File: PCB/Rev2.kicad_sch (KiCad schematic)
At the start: 80 parts, among them J1 AudioJack, J2 Conn_01x03_Socket, J3 Conn_01x02_Pin, U1 TL974, U2 LM78M05, U3 SN76489, U4 TL974, U5 MCP42010, U6 SN76489

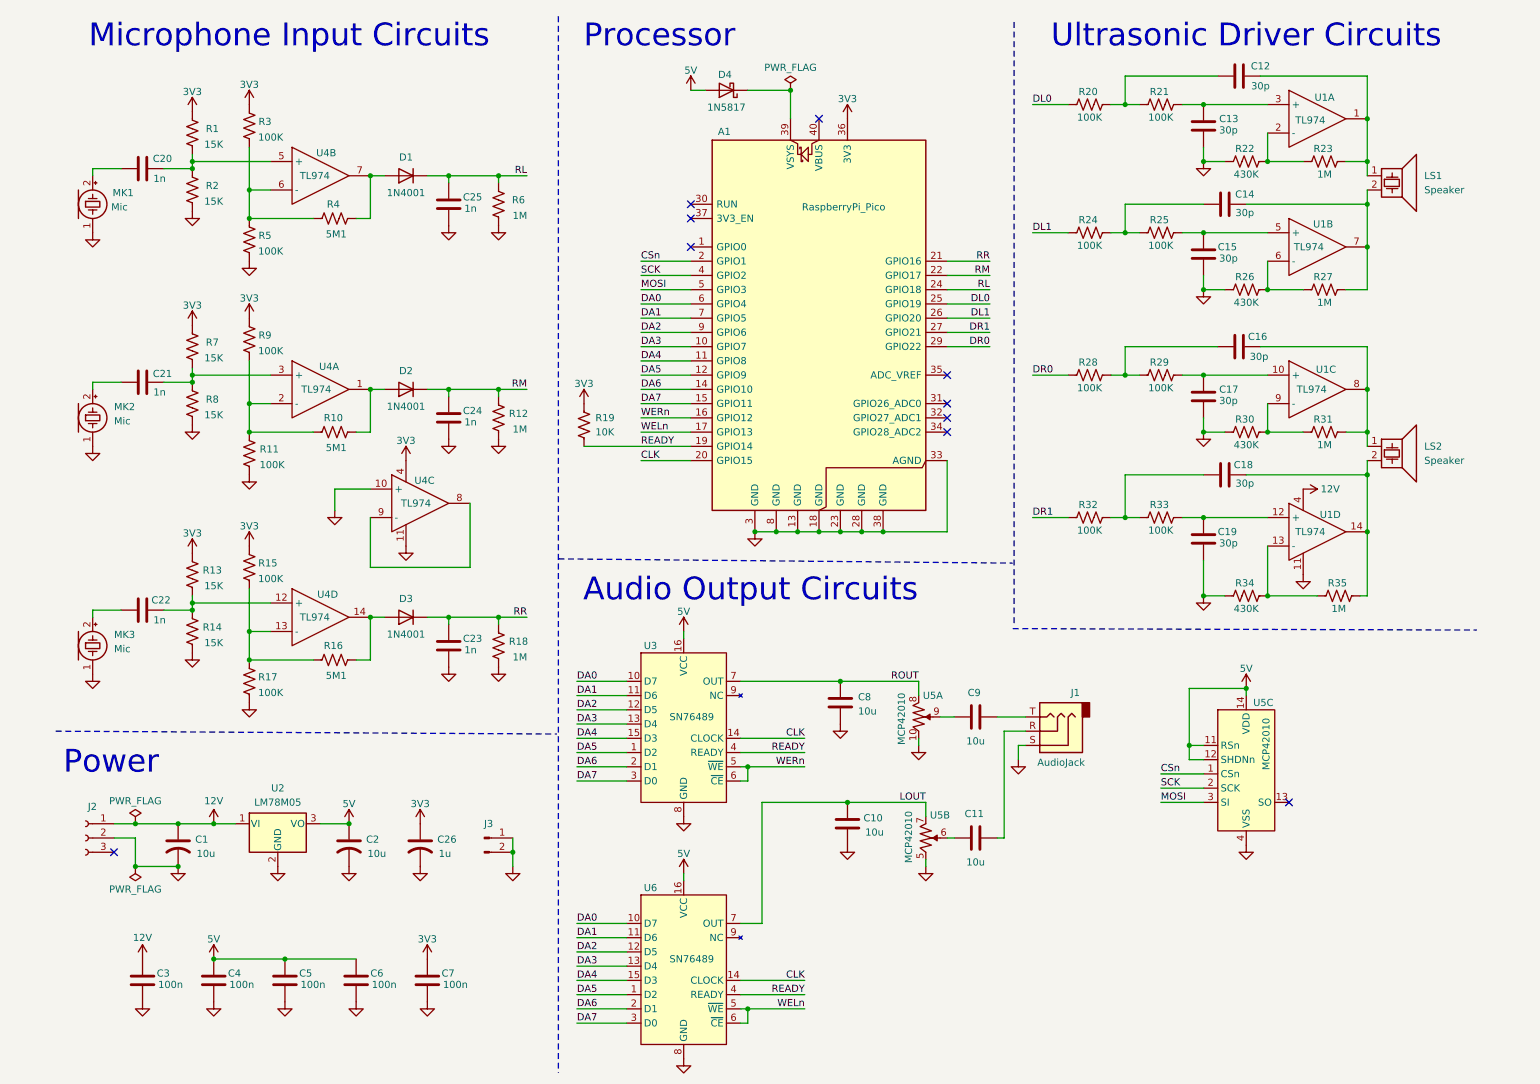
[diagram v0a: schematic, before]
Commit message: Doubled gain on receiver circuits.
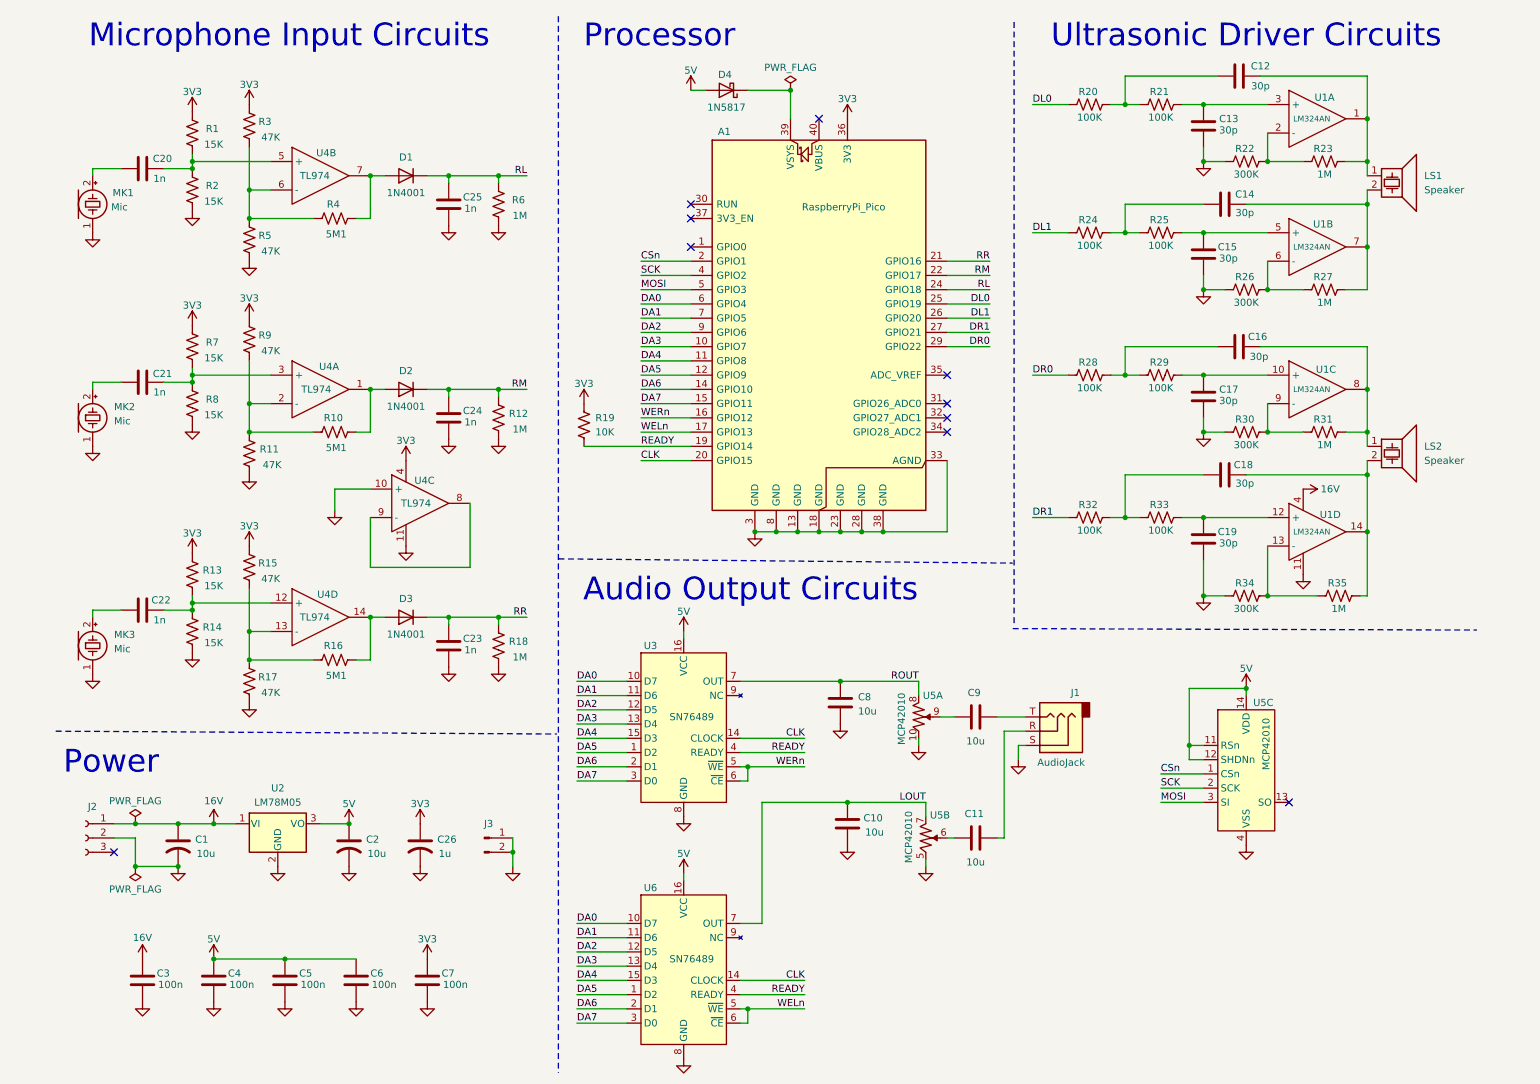
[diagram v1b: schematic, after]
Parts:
- R11, R15, R17, R3, R5, R9: value 100K -> 47K
- R22, R26, R30, R34: value 430K -> 300K
- U1: value TL974 -> LM324AN
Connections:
- net 12V renamed 16V
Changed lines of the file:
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@@
 		(title "Audio Theremin")
 		(date "2026-02-14")
-		(rev "2.0")
+		(rev "2.1")
 		(company "Christle Engineering")
 	)
@@
 			)
 		)
-		(property "Value" "TL974"
+		(property "Value" "LM324AN"
 			(at 236.474 81.28 0)
 			(show_name no)
@@
 			(effects
 				(font
-					(size 1.27 1.27)
+					(size 1.016 1.016)
 				)
 			)
@@
 			)
 		)
-		(property "Value" "TL974"
+		(property "Value" "LM324AN"
 			(at 233.934 106.68 0)
 			(hide yes)
@@
 			)
 		)
-		(property "Value" "TL974"
-			(at 235.966 55.88 0)
+		(property "Value" "LM324AN"
+			(at 236.474 55.88 0)
 			(show_name no)
 			(do_not_autoplace no)
 			(effects
 				(font
-					(size 1.27 1.27)
+					(size 1.016 1.016)
 				)
 			)
@@
 			)
 		)
-		(property "Value" "430K"
+		(property "Value" "300K"
 			(at 224.79 42.926 90)
 			(show_name no)
@@
 			)
 		)
-		(property "Value" "100K"
+		(property "Value" "47K"
 			(at 50.8 56.642 0)
 			(show_name no)
@@
 			)
 		)
-		(property "Value" "100K"
+		(property "Value" "47K"
 			(at 50.8 74.422 0)
 			(show_name no)
@@
 			)
 		)
-		(property "Value" "430K"
+		(property "Value" "300K"
 			(at 224.79 91.186 90)
 			(show_name no)
@@
 			)
 		)
-		(property "Value" "TL974"
-			(at 236.22 106.68 0)
+		(property "Value" "LM324AN"
+			(at 236.474 106.68 0)
 			(show_name no)
 			(do_not_autoplace no)
 			(effects
 				(font
-					(size 1.27 1.27)
+					(size 1.016 1.016)
 				)
 			)
@@
 			)
 		)
-		(property "Value" "TL974"
-			(at 236.22 33.274 0)
+		(property "Value" "LM324AN"
+			(at 236.474 33.02 0)
 			(show_name no)
 			(do_not_autoplace no)
 			(effects
 				(font
-					(size 1.27 1.27)
+					(size 1.016 1.016)
 				)
 			)
@@
 			)
 		)
-		(property "Value" "100K"
+		(property "Value" "47K"
 			(at 50.8 36.322 0)
 			(show_name no)
@@
 			)
 		)
-		(property "Value" "12V"
+		(property "Value" "16V"
 			(at 27.94 179.07 0)
 			(show_name no)
@@
 			)
 		)
-		(property "Value" "100K"
+		(property "Value" "47K"
 			(at 50.8 135.382 0)
 			(show_name no)
@@
 			)
 		)
-		(property "Value" "12V"
+		(property "Value" "16V"
 			(at 239.776 99.06 90)
 			(show_name no)
@@
 			)
 		)
-		(property "Value" "430K"
+		(property "Value" "300K"
 			(at 224.79 65.786 90)
 			(show_name no)
@@
 			)
 		)
-		(property "Value" "430K"
+		(property "Value" "300K"
 			(at 224.79 120.396 90)
 			(show_name no)
@@
 			)
 		)
-		(property "Value" "100K"
+		(property "Value" "47K"
 			(at 51.054 94.742 0)
 			(show_name no)
@@
 			)
 		)
-		(property "Value" "100K"
+		(property "Value" "47K"
 			(at 50.8 115.062 0)
 			(show_name no)
@@
 			)
 		)
-		(property "Value" "12V"
+		(property "Value" "16V"
 			(at 40.64 154.686 0)
 			(show_name no)

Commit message: Add files via upload
Changed default output voltage on receiver circuit. Added ground points, J4.
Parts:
- added J4: Conn_01x02_Pin, STFootPrints:PinHeader_1x02_P2.54mm_Vertical, symbol Connector:Conn_01x02_Pin
- R1, R13, R7: value 15K -> 56K
- R10, R16, R4: value 5M1 -> 1M8
- R11, R17, R5: value 47K -> 10K
- R14, R2, R8: value 15K -> 10K
- R15, R3, R9: value 47K -> 56K
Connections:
- net GND: now also J4.1 (Pin_1), J4.2 (Pin_2)
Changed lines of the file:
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@@
 		(title "Audio Theremin")
 		(date "2026-02-14")
-		(rev "2.1")
+		(rev "2.2")
 		(company "Christle Engineering")
 	)
@@
 	)
 	(junction
+		(at 93.98 177.8)
+		(diameter 0)
+		(color 0 0 0 0)
+	)
+	(junction
 		(at 34.29 166.37)
 		(diameter 0)
@@
 	(wire
 		(pts
+			(xy 93.98 177.8) (xy 93.98 180.34)
+		)
+		(stroke
+			(width 0)
+			(type default)
+		)
+	)
+	(wire
+		(pts
 			(xy 213.36 104.14) (xy 217.17 104.14)
 		)
@@
 	(wire
 		(pts
+			(xy 93.98 175.26) (xy 93.98 177.8)
+		)
+		(stroke
+			(width 0)
+			(type default)
+		)
+	)
+	(wire
+		(pts
 			(xy 138.43 154.94) (xy 153.67 154.94)
 		)
@@
 			)
 		)
-		(property "Value" "15K"
+		(property "Value" "56K"
 			(at 40.64 75.692 0)
 			(show_name no)
@@
 			)
 		)
-		(property "Value" "47K"
+		(property "Value" "10K"
 			(at 50.8 56.642 0)
 			(show_name no)
@@
 	)
 	(symbol
+		(lib_id "power:GND")
+		(at 93.98 180.34 0)
+		(unit 1)
+		(body_style 1)
+		(exclude_from_sim no)
+		(in_bom yes)
+		(on_board yes)
+		(in_pos_files yes)
+		(dnp no)
+		(fields_autoplaced yes)
+		(property "Reference" "#PWR062"
+			(at 93.98 186.69 0)
+			(hide yes)
+			(show_name no)
+			(do_not_autoplace no)
+			(effects
+				(font
+					(size 1.27 1.27)
+				)
+			)
+		)
+		(property "Value" "GND"
+			(at 93.98 185.42 0)
+			(hide yes)
+			(show_name no)
+			(do_not_autoplace no)
+			(effects
+				(font
+					(size 1.27 1.27)
+				)
+			)
+		)
+		(property "Footprint" ""
+			(at 93.98 180.34 0)
+			(hide yes)
+			(show_name no)
+			(do_not_autoplace no)
+			(effects
+				(font
+					(size 1.27 1.27)
+				)
+			)
+		)
+		(property "Datasheet" ""
+			(at 93.98 180.34 0)
+			(hide yes)
+			(show_name no)
+			(do_not_autoplace no)
+			(effects
+				(font
+					(size 1.27 1.27)
+				)
+			)
+		)
+		(property "Description" "Power symbol creates a global label with name \"GND\" , ground"
+			(at 93.98 180.34 0)
+			(hide yes)
+			(show_name no)
+			(do_not_autoplace no)
+			(effects
+				(font
+					(size 1.27 1.27)
+				)
+			)
+		)
+		(pin "1"
+		)
+		(instances
+			(project "Rev2"
+				(path "/e9471e7b-e883-42de-8fea-93c998677c96"
+					(reference "#PWR062")
+					(unit 1)
+				)
+			)
+		)
+	)
+	(symbol
 		(lib_id "Device:R_US")
 		(at 91.44 127 180)
@@
 			)
 		)
-		(property "Value" "5M1"
+		(property "Value" "1M8"
 			(at 62.484 132.334 90)
 			(show_name no)
@@
 			)
 		)
-		(property "Value" "15K"
+		(property "Value" "10K"
 			(at 40.64 47.752 0)
 			(show_name no)
@@
 			)
 		)
-		(property "Value" "47K"
+		(property "Value" "56K"
 			(at 50.8 74.422 0)
 			(show_name no)
@@
 			)
 		)
-		(property "Value" "15K"
+		(property "Value" "10K"
 			(at 40.64 126.492 0)
 			(show_name no)
@@
 			)
 		)
-		(property "Value" "15K"
+		(property "Value" "56K"
 			(at 40.64 37.592 0)
 			(show_name no)
@@
 			)
 		)
-		(property "Value" "15K"
+		(property "Value" "56K"
 			(at 40.64 116.332 0)
 			(show_name no)
@@
 			)
 		)
-		(property "Value" "47K"
+		(property "Value" "56K"
 			(at 50.8 36.322 0)
 			(show_name no)
@@
 	)
 	(symbol
+		(lib_id "Connector:Conn_01x02_Pin")
+		(at 88.9 175.26 0)
+		(unit 1)
+		(body_style 1)
+		(exclude_from_sim no)
+		(in_bom yes)
+		(on_board yes)
+		(in_pos_files yes)
+		(dnp no)
+		(property "Reference" "J4"
+			(at 89.662 172.72 0)
+			(show_name no)
+			(do_not_autoplace no)
+			(effects
+				(font
+					(size 1.27 1.27)
+				)
+			)
+		)
+		(property "Value" "Conn_01x02_Pin"
+			(at 89.535 172.72 0)
+			(hide yes)
+			(show_name no)
+			(do_not_autoplace no)
+			(effects
+				(font
+					(size 1.27 1.27)
+				)
+			)
+		)
+		(property "Footprint" "STFootPrints:PinHeader_1x02_P2.54mm_Vertical"
+			(at 88.9 175.26 0)
+			(hide yes)
+			(show_name no)
+			(do_not_autoplace no)
+			(effects
+				(font
+					(size 1.27 1.27)
+				)
+			)
+		)
+		(property "Datasheet" ""
+			(at 88.9 175.26 0)
+			(hide yes)
+			(show_name no)
+			(do_not_autoplace no)
+			(effects
+				(font
+					(size 1.27 1.27)
+				)
+			)
+		)
+		(property "Description" "Generic connector, single row, 01x02, script generated"
+			(at 88.9 175.26 0)
+			(hide yes)
+			(show_name no)
+			(do_not_autoplace no)
+			(effects
+				(font
+					(size 1.27 1.27)
+				)
+			)
+		)
+		(pin "1"
+		)
+		(pin "2"
+		)
+		(instances
+			(project "Rev2"
+				(path "/e9471e7b-e883-42de-8fea-93c998677c96"
+					(reference "J4")
+					(unit 1)
+				)
+			)
+		)
+	)
+	(symbol
 		(lib_id "Device:C_US")
 		(at 64.77 162.56 0)
@@
 			)
 		)
-		(property "Value" "47K"
+		(property "Value" "10K"
 			(at 50.8 135.382 0)
 			(show_name no)
@@
 			)
 		)
-		(property "Value" "5M1"
+		(property "Value" "1M8"
 			(at 62.484 53.594 90)
 			(show_name no)
@@
 			)
 		)
-		(property "Value" "15K"
+		(property "Value" "10K"
 			(at 40.64 85.852 0)
 			(show_name no)
@@
 			)
 		)
-		(property "Value" "5M1"
+		(property "Value" "1M8"
 			(at 62.484 91.694 90)
 			(show_name no)
@@
 			)
 		)
-		(property "Value" "47K"
+		(property "Value" "10K"
 			(at 51.054 94.742 0)
 			(show_name no)
@@
 			)
 		)
-		(property "Value" "47K"
+		(property "Value" "56K"
 			(at 50.8 115.062 0)
 			(show_name no)
